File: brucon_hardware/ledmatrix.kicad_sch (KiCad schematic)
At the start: 270 parts, among them U301 TC7258E, U302 TC5020D, U303 TC5020D, U304 TC5020D, U305 TC5020D, U306 TC5020D, U307 TC5020D, U308 74HCT245

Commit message: Updated led matrix
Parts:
- removed D301, D302, D303, D304, D305, D306, D307, D308, D309, D310, D311, D312, D313, D314, D315, D316, D317, D318, D319, D320, D321, D322, D323, D324, D325, D326, D327, D328, D329, D330, D331, D332, D333, D334, D335, D336, D337, D338, D339, D340, D341, D342, D343, D344, D345, D346, D347, D348, D349, D350, D351, D352, D353, D354, D355, D356, D357, D358, D359, D360, D361, D362, D363, D364, D365, D366, D367, D368, D369, D370, D371, D372, D373, D374, D375, D376, D377, D378, D379, D380, D381, D382, D383, D384, D385, D386, D387, D388, D389, D390, D391, D392, D393, D394, D395, D396, D397, D398, D399, D400, D401, D402, D403, D404, D405, D406, D407, D408, D409, D410, D411, D412, D413, D414, D415, D416, D417, D418, D419, D420, D421, D422, D423, D424, D425, D426, D427, D428, D429, D430, D431, D432, D433, D434, D435, D436, D437, D438, D439, D440, D441, D442, D443, D444, D445, D446, D447, D448, D449, D450, D451, D452, D453, D454, D455, D456, D457, D458, D459, D460, D461, D462, D463, D464, D465, D466, D467, D468, D469, D470, D471, D472, D473, D474, D475, D476, D477, D478, D479, D480, D481, D482, D483, D484, D485, D486, D487, D488, D489, D490, D491, D492, D493, D494, D495, D496, D497, D498, D499, D500, D501, D502, D503, D504, D505, D506, D507, D508, D509, D510, D511, D512, D513, D514, D515, D516, D517, D518, D519, D520, D521, D522, D523, D524, D525, D526, D527, D528, D529, D530, D531, D532, D533, D534, D535, D536, D537, D538, D539, D540, D541, D542, D543, D544, D545, D546, D547, D548, D549, D550, D551, D552, D553, D554, D555, D556: LL-R3528RGBC-008-B, LED_SMD:LED_Cree-PLCC4_3.2x2.8mm_CCW, symbol led_rgba:LED_RGBA
- added U303, U304: TC7258E, Package_SO:SOIC-16_3.9x9.9mm_P1.27mm, symbol rgbchip:TC7258E
- renumbered U308 to U301, U301 to U302, U302 to U305, U303 to U306, U304 to U307, U305 to U308, U306 to U309, U307 to U310
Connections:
- net +5V: now also U303.1 (VDD), U303.7 (ENH), U303.9 (VDD), U304.1 (VDD), U304.7 (ENH), U304.9 (VDD)
- net GND: now also U303.8 (GND), U304.8 (GND)
- net OE: no longer U301.9 (A7)
- net led_row18/R: now reaches U308.7 (OUT2)
- net led_row18/G: now reaches U309.7 (OUT2)
- net led_row18/B: now reaches U310.7 (OUT2)
- net ROW.LINE0: now reaches U302.3 (OUT1)
- net led_row5/R: now reaches U305.10 (OUT5)
- net led_row5/G: now reaches U306.10 (OUT5)
- net led_row5/B: now reaches U307.10 (OUT5)
- net ROW.LINE7: now reaches U302.14 (OUT8)
- net led_row12/R: now reaches U305.17 (OUT12)
- net led_row12/G: now reaches U306.17 (OUT12)
- net led_row12/B: now reaches U307.17 (OUT12)
- net ROW.LINE4: now reaches U302.11 (OUT5)
- net led_row20/R: now reaches U308.9 (OUT4)
- net led_row20/G: now reaches U309.9 (OUT4)
- net led_row20/B: now reaches U310.9 (OUT4)
- net ROW.LINE5: now reaches U302.12 (OUT6)
- net led_row28/R: now reaches U308.17 (OUT12)
- net led_row28/G: now reaches U309.17 (OUT12)
- net led_row28/B: now reaches U310.17 (OUT12)
- net ROW.LINE6: now reaches U302.13 (OUT7)
- net led_row17/R: now reaches U308.6 (OUT1)
- net led_row17/G: now reaches U309.6 (OUT1)
- net led_row17/B: now reaches U310.6 (OUT1)
- net led_row14/R: now reaches U305.19 (OUT14)
- net led_row14/G: now reaches U306.19 (OUT14)
- net led_row14/B: now reaches U307.19 (OUT14)
- net led_row27/R: now reaches U308.16 (OUT11)
- net led_row27/G: now reaches U309.16 (OUT11)
- net led_row27/B: now reaches U310.16 (OUT11)
- net led_row25/R: now reaches U308.14 (OUT9)
- net led_row25/G: now reaches U309.14 (OUT9)
- net led_row25/B: now reaches U310.14 (OUT9)
- net led_row8/R: now reaches U305.13 (OUT8)
- net led_row8/G: now reaches U306.13 (OUT8)
- net led_row8/B: now reaches U307.13 (OUT8)
- net led_row23/R: now reaches U308.12 (OUT7)
- net led_row23/G: now reaches U309.12 (OUT7)
- net led_row23/B: now reaches U310.12 (OUT7)
- net ROW.LINE3: now reaches U302.6 (OUT4)
- net ROW.LINE3: now also U302.5 (OUT3)
- net led_row1/R: now reaches U305.6 (OUT1)
- net led_row1/G: now reaches U306.6 (OUT1)
- net led_row1/B: now reaches U307.6 (OUT1)
- net led_row7/R: now reaches U305.12 (OUT7)
- net led_row7/G: now reaches U306.12 (OUT7)
- net led_row7/B: now reaches U307.12 (OUT7)
- net led_row6/R: now reaches U305.11 (OUT6)
- net led_row6/G: now reaches U306.11 (OUT6)
- net led_row6/B: now reaches U307.11 (OUT6)
- net ROW.LINE1: now reaches U302.4 (OUT2)
- net led_row24/R: now reaches U308.13 (OUT8)
- net led_row24/G: now reaches U309.13 (OUT8)
- net led_row24/B: now reaches U310.13 (OUT8)
- net led_row29/R: now reaches U308.18 (OUT13)
- net led_row29/G: now reaches U309.18 (OUT13)
- net led_row29/B: now reaches U310.18 (OUT13)
- net led_row0/R: now reaches U305.5 (OUT0)
- net led_row0/G: now reaches U306.5 (OUT0)
- net led_row0/B: now reaches U307.5 (OUT0)
- net led_row4/R: now reaches U305.9 (OUT4)
- net led_row4/G: now reaches U306.9 (OUT4)
- net led_row4/B: now reaches U307.9 (OUT4)
- net led_row16/R: now reaches U308.5 (OUT0)
- net led_row16/G: now reaches U309.5 (OUT0)
- net led_row16/B: now reaches U310.5 (OUT0)
- net led_row3/R: now reaches U305.8 (OUT3)
- net led_row3/G: now reaches U306.8 (OUT3)
- net led_row3/B: now reaches U307.8 (OUT3)
- net at U301.11 (B7): now also U304.10 (ENL); no longer U302.10 (ENL)
- net at U301.18 (B0), U302.15 (A): now also U303.15 (A), U304.15 (A)
- net at U301.17 (B1), U302.16 (B): now also U303.16 (B), U304.16 (B)
- net at U301.16 (B2), U302.2 (C): now also U303.2 (C), U304.2 (C)
- net led_row9/R: now reaches U305.14 (OUT9)
- net led_row9/G: now reaches U306.14 (OUT9)
- net led_row9/B: now reaches U307.14 (OUT9)
- net led_row19/R: now reaches U308.8 (OUT3)
- net led_row19/G: now reaches U309.8 (OUT3)
- net led_row19/B: now reaches U310.8 (OUT3)
- net led_row15/R: now reaches U305.20 (OUT15)
- net led_row15/G: now reaches U306.20 (OUT15)
- net led_row15/B: now reaches U307.20 (OUT15)
- net led_row21/R: now reaches U308.10 (OUT5)
- net led_row21/G: now reaches U309.10 (OUT5)
- net led_row21/B: now reaches U310.10 (OUT5)
- net led_row2/R: now reaches U305.7 (OUT2)
- net led_row2/G: now reaches U306.7 (OUT2)
- net led_row2/B: now reaches U307.7 (OUT2)
- net led_row22/G: now reaches U309.11 (OUT6)
- net led_row26/G: now reaches U309.15 (OUT10)
- net led_row30/G: now reaches U309.19 (OUT14)
- net led_row31/G: now reaches U309.20 (OUT15)
- net led_row13/R: now reaches U305.18 (OUT13)
- net led_row13/G: now reaches U306.18 (OUT13)
- net led_row13/B: now reaches U307.18 (OUT13)
- net led_row11/R: now reaches U305.16 (OUT11)
- net led_row11/G: now reaches U306.16 (OUT11)
- net led_row11/B: now reaches U307.16 (OUT11)
- net led_row26/R: now reaches U308.15 (OUT10)
- net led_row26/B: now reaches U310.15 (OUT10)
- net led_row30/R: now reaches U308.19 (OUT14)
- net led_row30/B: now reaches U310.19 (OUT14)
- net led_row31/R: now reaches U308.20 (OUT15)
- net led_row31/B: now reaches U310.20 (OUT15)
- net led_row22/R: now reaches U308.11 (OUT6)
- net led_row22/B: now reaches U310.11 (OUT6)
- net led_row10/R: now reaches U305.15 (OUT10)
- net led_row10/G: now reaches U306.15 (OUT10)
- net led_row10/B: now reaches U307.15 (OUT10)
- net at U301.12 (B6): now also U303.10 (ENL)
- net at U301.13 (B5): now also U302.10 (ENL)
- net OE0: now reaches U301.7 (A5)
- net OE1: now reaches U301.8 (A6)
- new net OE2: U301.9 (A7)
- new net ROW.LINE10: U303.5 (OUT3)
- new net ROW.LINE11: U303.6 (OUT4)
- new net ROW.LINE12: U303.11 (OUT5)
- new net ROW.LINE13: U303.12 (OUT6)
- new net ROW.LINE14: U303.13 (OUT7)
- new net ROW.LINE15: U303.14 (OUT8)
- new net ROW.LINE16: U304.3 (OUT1)
- new net ROW.LINE17: U304.4 (OUT2)
- new net ROW.LINE18: U304.5 (OUT3)
- new net ROW.LINE8: U303.3 (OUT1)
- new net ROW.LINE9: U303.4 (OUT2)
- no-connect marks 11 -> 12
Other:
- added sheet led_row0 (row.kicad_sch)
- added sheet led_row1 (row.kicad_sch)
- added sheet led_row10 (row.kicad_sch)
- added sheet led_row11 (row.kicad_sch)
- added sheet led_row12 (row.kicad_sch)
- added sheet led_row13 (row.kicad_sch)
- added sheet led_row14 (row.kicad_sch)
- added sheet led_row15 (row.kicad_sch)
- added sheet led_row16 (row.kicad_sch)
- added sheet led_row17 (row.kicad_sch)
- added sheet led_row18 (row.kicad_sch)
- added sheet led_row19 (row.kicad_sch)
- added sheet led_row2 (row.kicad_sch)
- added sheet led_row20 (row.kicad_sch)
- added sheet led_row21 (row.kicad_sch)
- added sheet led_row22 (row.kicad_sch)
- added sheet led_row23 (row.kicad_sch)
- added sheet led_row24 (row.kicad_sch)
- added sheet led_row25 (row.kicad_sch)
- added sheet led_row26 (row.kicad_sch)
- added sheet led_row27 (row.kicad_sch)
- added sheet led_row28 (row.kicad_sch)
- added sheet led_row29 (row.kicad_sch)
- added sheet led_row3 (row.kicad_sch)
- added sheet led_row30 (row.kicad_sch)
- added sheet led_row31 (row.kicad_sch)
- added sheet led_row4 (row.kicad_sch)
- added sheet led_row5 (row.kicad_sch)
- added sheet led_row6 (row.kicad_sch)
- added sheet led_row7 (row.kicad_sch)
- added sheet led_row8 (row.kicad_sch)
- added sheet led_row9 (row.kicad_sch)

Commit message: Updated bom
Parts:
- R301, R302, R303, R304, R305, R306: LCSC (none) -> C23179
- U301: footprint (none) -> Package_SO:TSSOP-20_4.4x6.5mm_P0.65mm; LCSC (none) -> C7494911
- U302, U303, U304: value TC7258E -> TC7262C; footprint Package_SO:SOIC-16_3.9x9.9mm_P1.27mm -> Package_SO:SO-16_3.9x9.9mm_P1.27mm; LCSC (none) -> C2887471
- U305, U306, U307, U308, U309, U310: LCSC (none) -> C18221482
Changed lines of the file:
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@@
+      (effects (font (size 1.27 1.27)) hide)
+    )
+    (property "LCSC" "C23179" (at 994.41 270.51 0)
       (effects (font (size 1.27 1.27)) hide)
     )
@@
       (effects (font (size 1.27 1.27)))
     )
-    (property "Value" "TC7258E" (at 370.4336 519.43 0)
-      (effects (font (size 1.27 1.27)))
-    )
-    (property "Footprint" "Package_SO:SOIC-16_3.9x9.9mm_P1.27mm" (at 369.57 519.43 0)
+    (property "Value" "TC7262C" (at 370.4336 519.43 0)
+      (effects (font (size 1.27 1.27)))
+    )
+    (property "Footprint" "Package_SO:SO-16_3.9x9.9mm_P1.27mm" (at 369.57 519.43 0)
       (effects (font (size 1.27 1.27)) hide)
     )
     (property "Datasheet" "http://www.superchip.cn/Private/ProductFiles/6364584403048069321406626239.pdf" (at 369.57 519.43 0)
+      (effects (font (size 1.27 1.27)) hide)
+    )
+    (property "LCSC" "C2887471" (at 369.57 519.43 0)
       (effects (font (size 1.27 1.27)) hide)
     )
@@
       (effects (font (size 1.27 1.27)) hide)
     )
+    (property "LCSC" "C23179" (at 991.87 140.97 0)
+      (effects (font (size 1.27 1.27)) hide)
+    )
     (pin "1")
     (pin "2")
@@
       (effects (font (size 1.27 1.27)))
     )
-    (property "Value" "TC7258E" (at 370.4336 415.29 0)
-      (effects (font (size 1.27 1.27)))
-    )
-    (property "Footprint" "Package_SO:SOIC-16_3.9x9.9mm_P1.27mm" (at 369.57 415.29 0)
+    (property "Value" "TC7262C" (at 370.4336 415.29 0)
+      (effects (font (size 1.27 1.27)))
+    )
+    (property "Footprint" "Package_SO:SO-16_3.9x9.9mm_P1.27mm" (at 369.57 415.29 0)
       (effects (font (size 1.27 1.27)) hide)
     )
     (property "Datasheet" "http://www.superchip.cn/Private/ProductFiles/6364584403048069321406626239.pdf" (at 369.57 415.29 0)
+      (effects (font (size 1.27 1.27)) hide)
+    )
+    (property "LCSC" "C2887471" (at 369.57 415.29 0)
       (effects (font (size 1.27 1.27)) hide)
     )
@@
       (effects (font (size 1.27 1.27)) hide)
     )
+    (property "LCSC" "C23179" (at 990.6 100.33 0)
+      (effects (font (size 1.27 1.27)) hide)
+    )
     (pin "1")
     (pin "2")
@@
     )
     (property "Datasheet" "" (at 991.87 228.6 0)
+      (effects (font (size 1.27 1.27)) hide)
+    )
+    (property "LCSC" "C18221482" (at 991.87 228.6 0)
       (effects (font (size 1.27 1.27)) hide)
     )
@@
       (effects (font (size 1.27 1.27)) hide)
     )
+    (property "LCSC" "C23179" (at 993.14 229.87 0)
+      (effects (font (size 1.27 1.27)) hide)
+    )
     (pin "1")
     (pin "2")
@@
     )
     (property "Datasheet" "https://datasheet.lcsc.com/szlcsc/Shenzhen-Mingwei-Elec-SM16106SC_C121618.pdf" (at 990.6 187.96 0)
+      (effects (font (size 1.27 1.27)) hide)
+    )
+    (property "LCSC" "C18221482" (at 990.6 187.96 0)
       (effects (font (size 1.27 1.27)) hide)
     )
@@
       (effects (font (size 1.27 1.27)) hide)
     )
+    (property "LCSC" "C18221482" (at 988.06 58.42 0)
+      (effects (font (size 1.27 1.27)) hide)
+    )
     (pin "1")
     (pin "10")
@@
       (effects (font (size 1.27 1.27)) hide)
     )
+    (property "LCSC" "C18221482" (at 990.6 139.7 0)
+      (effects (font (size 1.27 1.27)) hide)
+    )
     (pin "1")
     (pin "10")
@@
       (effects (font (size 1.27 1.27)) hide)
     )
+    (property "LCSC" "C23179" (at 989.33 59.69 0)
+      (effects (font (size 1.27 1.27)) hide)
+    )
     (pin "1")
     (pin "2")
@@
       (effects (font (size 1.27 1.27)) (justify left))
     )
-    (property "Footprint" "" (at 313.69 450.85 0)
+    (property "Footprint" "Package_SO:TSSOP-20_4.4x6.5mm_P0.65mm" (at 313.69 450.85 0)
       (effects (font (size 1.27 1.27)) hide)
     )
     (property "Datasheet" "http://www.ti.com/lit/gpn/sn74HC245" (at 313.69 450.85 0)
+      (effects (font (size 1.27 1.27)) hide)
+    )
+    (property "LCSC" "C7494911" (at 313.69 450.85 0)
       (effects (font (size 1.27 1.27)) hide)
     )
@@
       (effects (font (size 1.27 1.27)) hide)
     )
+    (property "LCSC" "C23179" (at 991.87 189.23 0)
+      (effects (font (size 1.27 1.27)) hide)
+    )
     (pin "1")
     (pin "2")
@@
       (effects (font (size 1.27 1.27)))
     )
-    (property "Value" "TC7258E" (at 370.4336 467.36 0)
-      (effects (font (size 1.27 1.27)))
-    )
-    (property "Footprint" "Package_SO:SOIC-16_3.9x9.9mm_P1.27mm" (at 369.57 467.36 0)
+    (property "Value" "TC7262C" (at 370.4336 467.36 0)
+      (effects (font (size 1.27 1.27)))
+    )
+    (property "Footprint" "Package_SO:SO-16_3.9x9.9mm_P1.27mm" (at 369.57 467.36 0)
       (effects (font (size 1.27 1.27)) hide)
     )
     (property "Datasheet" "http://www.superchip.cn/Private/ProductFiles/6364584403048069321406626239.pdf" (at 369.57 467.36 0)
+      (effects (font (size 1.27 1.27)) hide)
+    )
+    (property "LCSC" "C2887471" (at 369.57 467.36 0)
       (effects (font (size 1.27 1.27)) hide)
     )
@@
     )
     (property "Datasheet" "" (at 993.14 269.24 0)
+      (effects (font (size 1.27 1.27)) hide)
+    )
+    (property "LCSC" "C18221482" (at 993.14 269.24 0)
       (effects (font (size 1.27 1.27)) hide)
     )
@@
       (effects (font (size 1.27 1.27)) hide)
     )
+    (property "LCSC" "C18221482" (at 989.33 99.06 0)
+      (effects (font (size 1.27 1.27)) hide)
+    )

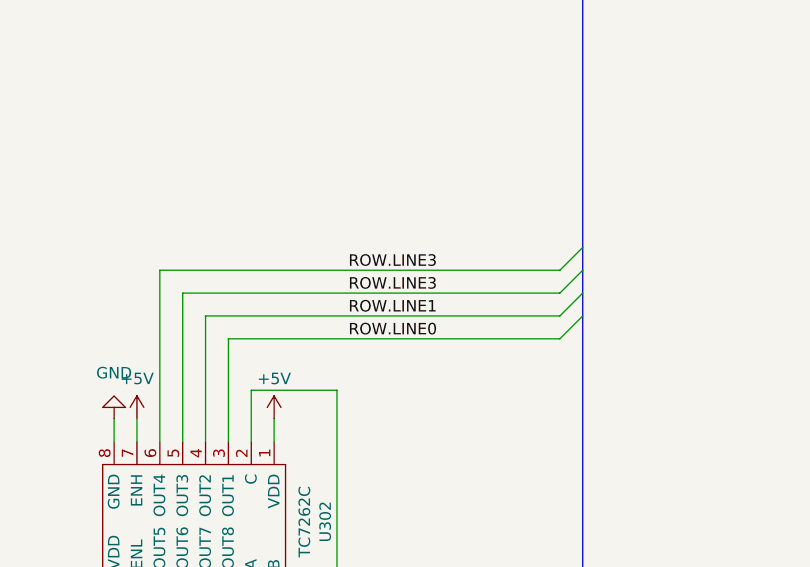
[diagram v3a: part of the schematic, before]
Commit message: Finished major parts routing led matrix
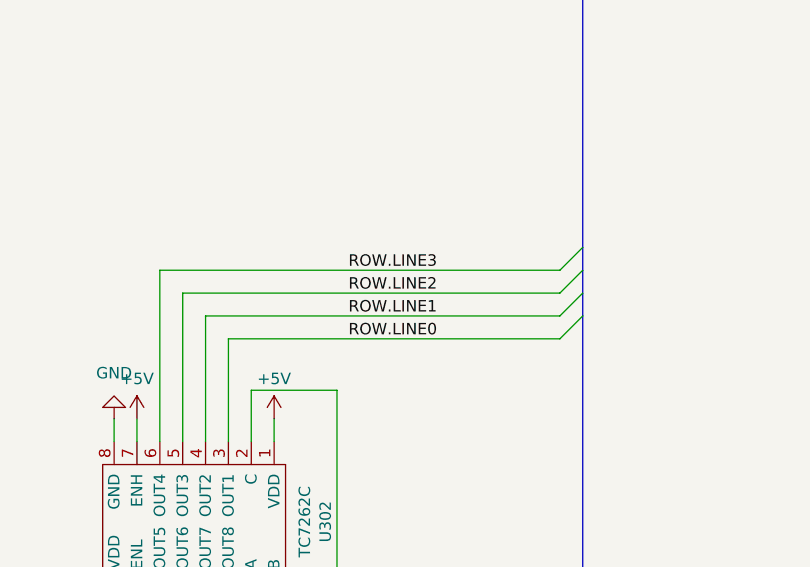
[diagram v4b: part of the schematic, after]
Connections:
- net ROW.LINE3: no longer U302.5 (OUT3)
- new net ROW.LINE2: U302.5 (OUT3)
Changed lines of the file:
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@@
     (effects (font (size 1.27 1.27)) (justify left bottom))
   )
-  (label "ROW.LINE3" (at 375.285 389.89 0) (fields_autoplaced)
+  (label "ROW.LINE2" (at 375.285 389.89 0) (fields_autoplaced)
     (effects (font (size 1.27 1.27)) (justify left bottom))
   )

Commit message: Major parts routed
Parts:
- added C301, C302, C303, C304, C305, C306, C307, C308, C309: 100nF, Capacitor_SMD:C_0603_1608Metric, symbol Device:C
- R301, R302, R303, R304, R305, R306: footprint Resistor_SMD:R_0603_1608Metric -> Resistor_SMD:R_0402_1005Metric
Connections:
- net +3.3V: now also C301.1, C302.1, C303.1, C304.1, C305.1, C306.1
- net +5V: now also C307.1, C308.1, C309.1
- net GND: now also C301.2, C302.2, C303.2, C304.2, C305.2, C306.2, C307.2, C308.2, C309.2
- net at U304.10 (ENL): now also U301.13 (B5); no longer U301.11 (B7)
- net at U302.10 (ENL): now also U301.11 (B7); no longer U301.13 (B5)

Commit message: Updated hardware
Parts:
- R301, R302, R303, R304, R305, R306: value 470 -> 1.8k; LCSC C23179 -> (none)
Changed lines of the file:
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@@
 			)
 		)
-		(property "Value" "470"
+		(property "Value" "1.8k"
 			(at 996.188 271.653 0)
 			(effects
@@
 			)
 		)
-		(property "LCSC" "C23179"
+		(property "LCSC" ""
 			(at 994.41 270.51 0)
 			(effects
@@
 			)
 		)
-		(property "Value" "470"
+		(property "Value" "1.8k"
 			(at 993.648 142.113 0)
 			(effects
@@
 			)
 		)
-		(property "LCSC" "C23179"
+		(property "LCSC" ""
 			(at 991.87 140.97 0)
 			(effects
@@
 			)
 		)
-		(property "Value" "470"
+		(property "Value" "1.8k"
 			(at 992.378 101.473 0)
 			(effects
@@
 			)
 		)
-		(property "LCSC" "C23179"
+		(property "LCSC" ""
 			(at 990.6 100.33 0)
 			(effects
@@
 			)
 		)
-		(property "Value" "470"
+		(property "Value" "1.8k"
 			(at 994.918 231.013 0)
 			(effects
@@
 			)
 		)
-		(property "LCSC" "C23179"
+		(property "LCSC" ""
 			(at 993.14 229.87 0)
 			(effects
@@
 			)
 		)
-		(property "Value" "470"
+		(property "Value" "1.8k"
 			(at 991.108 60.833 0)
 			(effects
@@
 			)
 		)
-		(property "LCSC" "C23179"
+		(property "LCSC" ""
 			(at 989.33 59.69 0)
 			(effects
@@
 			)
 		)
-		(property "Value" "470"
+		(property "Value" "1.8k"
 			(at 993.648 190.373 0)
 			(effects
@@
 			)
 		)
-		(property "LCSC" "C23179"
+		(property "LCSC" ""
 			(at 991.87 189.23 0)
 			(effects
